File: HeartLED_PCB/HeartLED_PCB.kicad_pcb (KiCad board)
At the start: 2 copper layers, 58.8 x 52.2 mm, 35 parts, among them U1 ICM7555CBAZ, U2 CD4017BM, U3 HT7750A, U4 HX SS12F44G4

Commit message: Added LCSC and 3D models
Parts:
- C3: footprint FOOTPRINTS:TAJA476K006RNJ -> FOOTPRINTS:TAJA226M010RNJ
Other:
- board text added: "github.com/ fectec/ HeartLED"
- board text removed: "github.com/ fectec/ HeartLEDChaser"

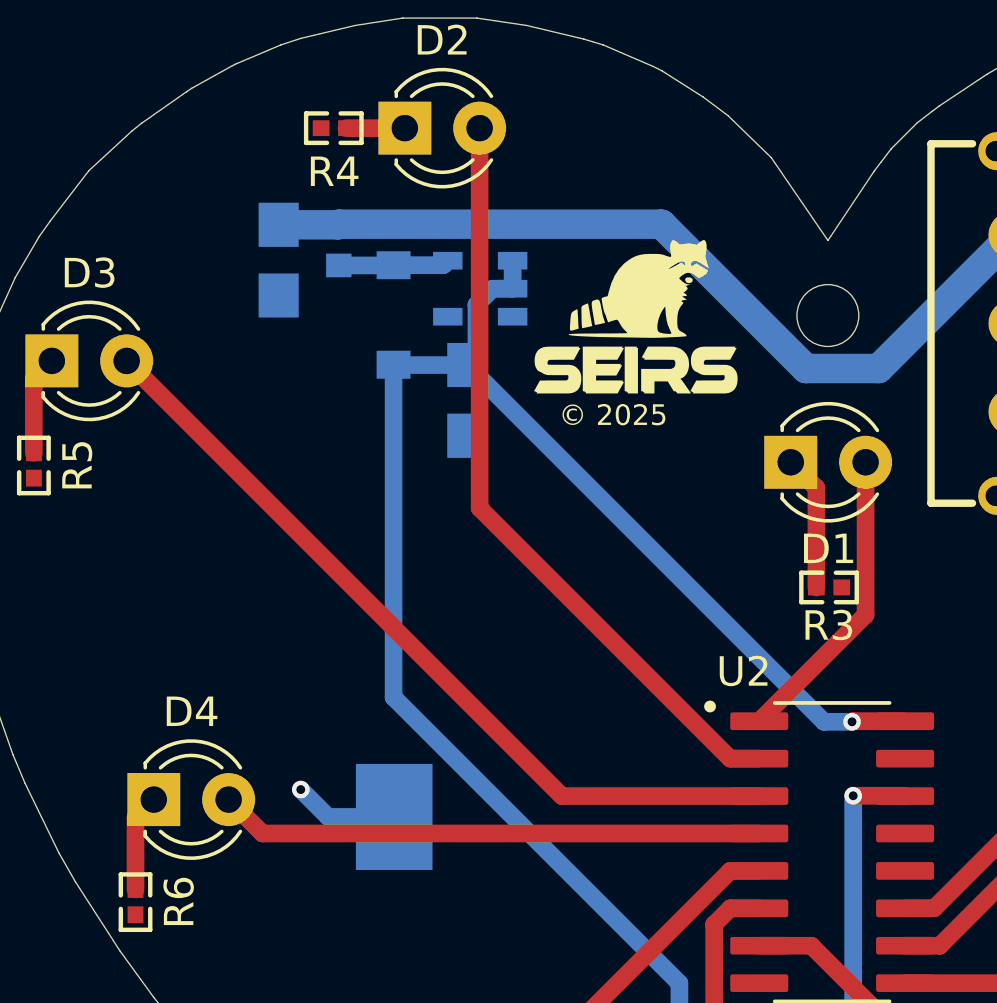
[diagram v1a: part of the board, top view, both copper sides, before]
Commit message: Changed inductor
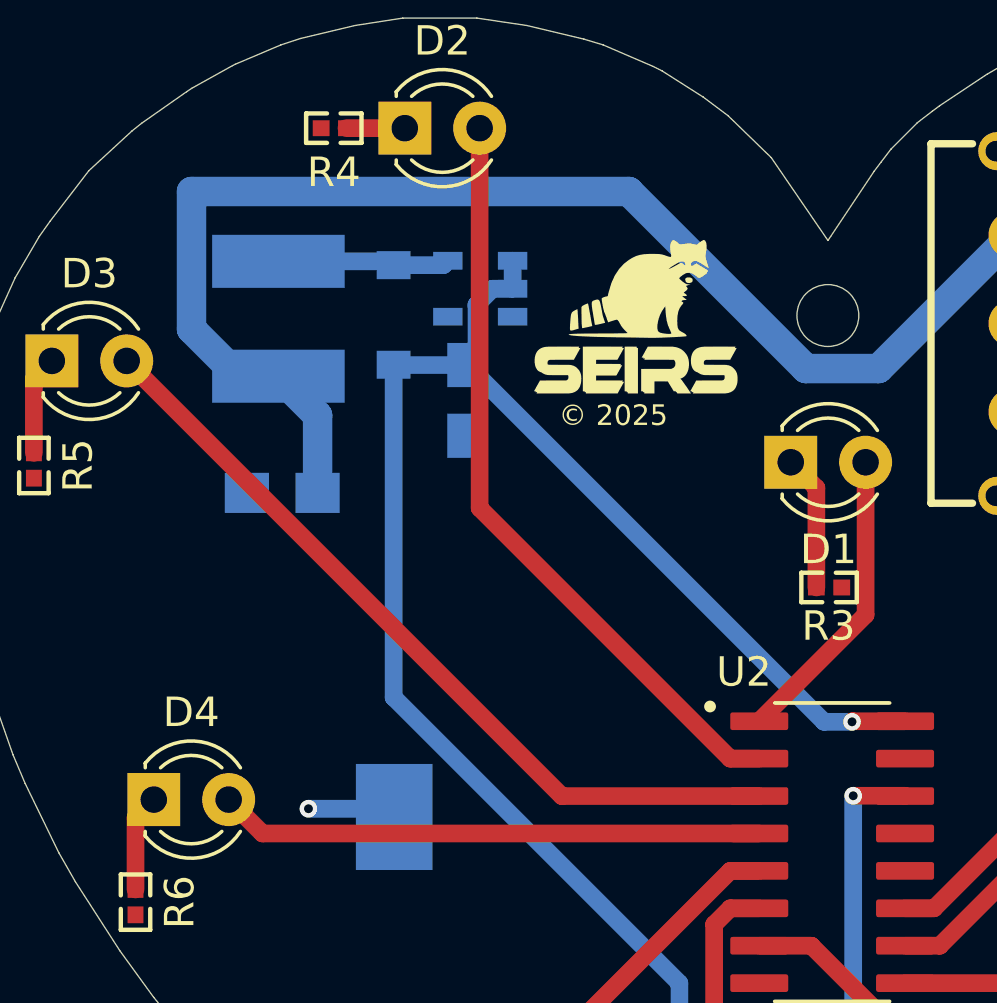
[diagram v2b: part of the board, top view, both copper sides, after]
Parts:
- L1: footprint FOOTPRINTS:SDFL1608Q4R7KTF -> FOOTPRINTS:SMNR5040-470MT
- moved C2 7.90 mm to (111.5, 88.6), turned to 180 degrees
- moved L1 3.24 mm to (111.3, 82.7), turned to 90 degrees
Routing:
- net +3V0: track 28.8 -> 43.7 mm
- net Net-(S1-A): track 3.75 -> 5.68 mm
- net GND: track 3.56 -> 3.03 mm

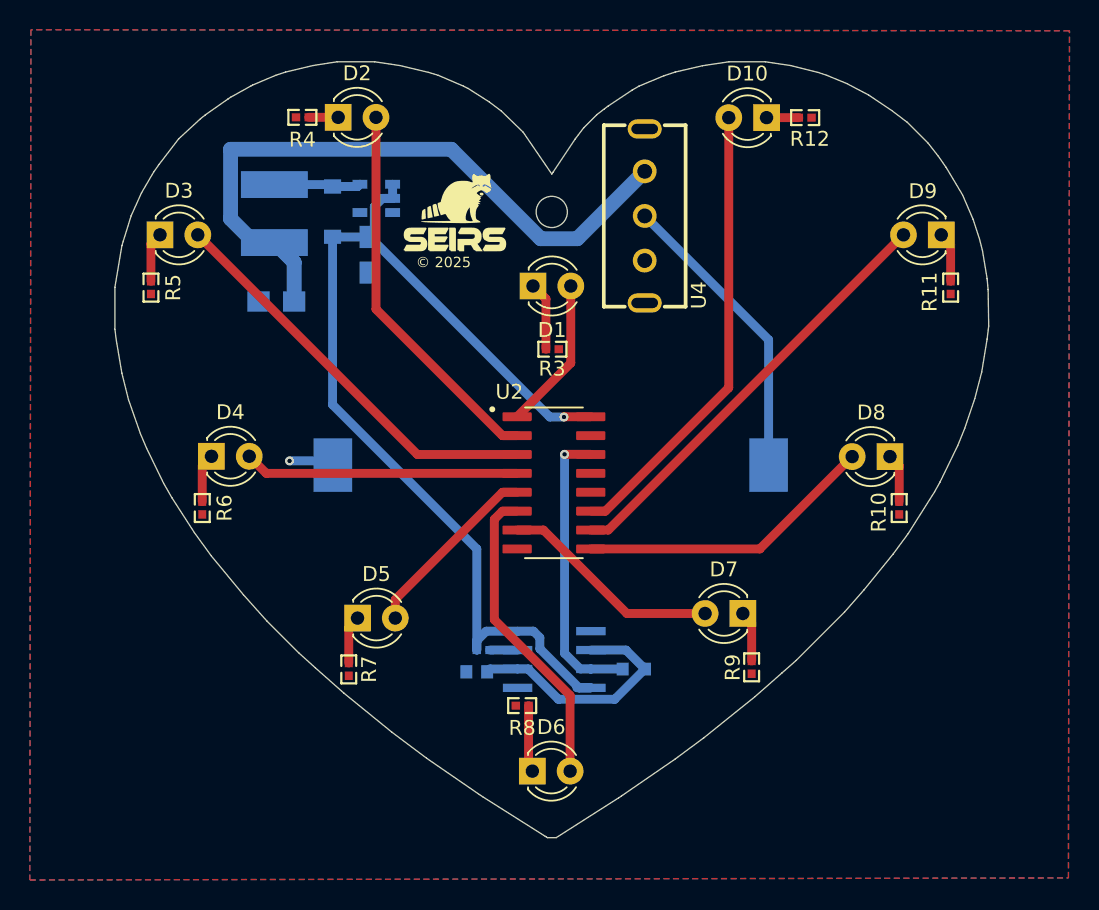
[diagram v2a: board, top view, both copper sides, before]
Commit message: Added TestPoints and corrected track width for power nets
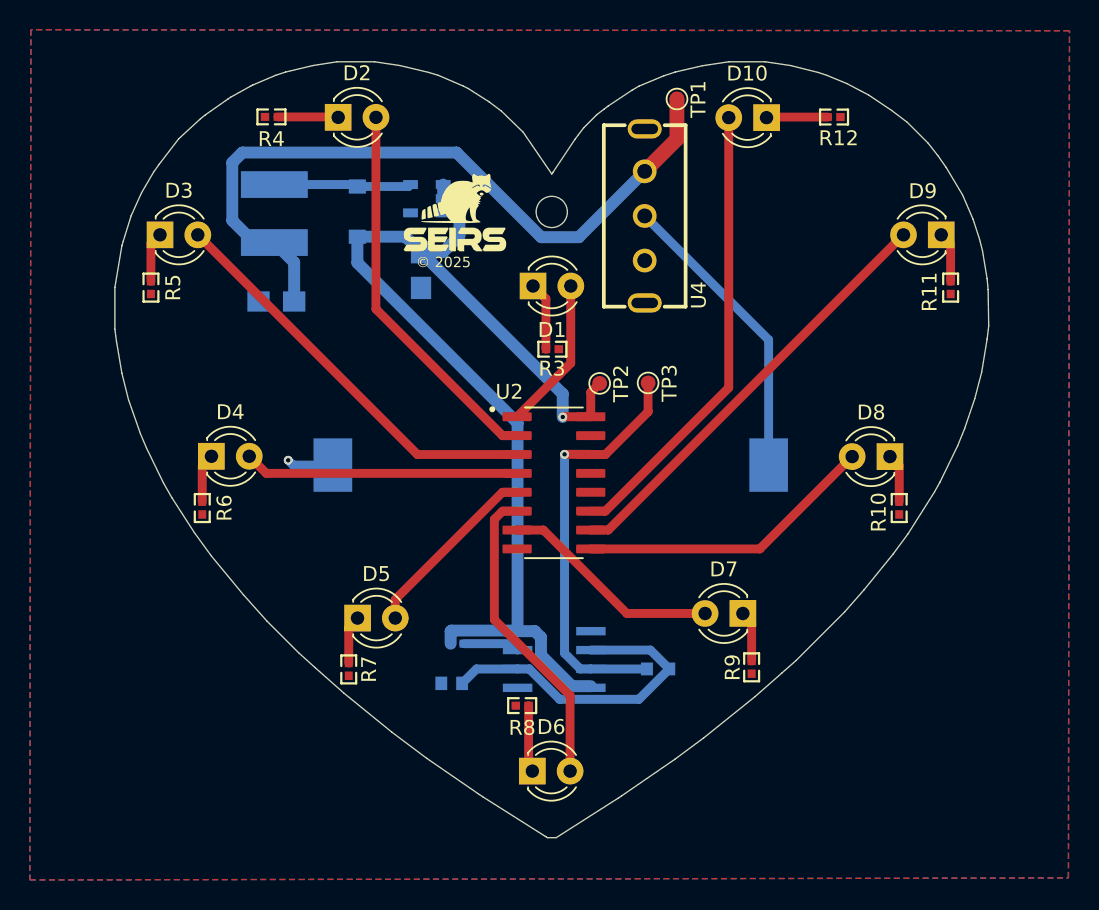
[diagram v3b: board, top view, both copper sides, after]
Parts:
- added TP1: TestPoint, TestPoint:TestPoint_Pad_D1.0mm, F.Cu at (138.4, 75.0)
- added TP2: TestPoint, TestPoint:TestPoint_Pad_D1.0mm, F.Cu at (133.2, 94.1)
- added TP3: TestPoint, TestPoint:TestPoint_Pad_D1.0mm, F.Cu at (136.5, 94.1)
- moved C3 3.60 mm to (121.2, 86.5)
- moved U3 3.40 mm to (121.6, 81.7)
- moved R4 2.08 mm to (111.2, 76.2)
- moved R12 1.94 mm to (149.0, 76.2)
- moved C1 1.86 mm to (123.3, 114.3)
- moved R2 1.79 mm to (123.7, 111.6)
- moved S1 1.67 mm to (116.9, 82.6)
- moved R1 1.63 mm to (137.2, 113.3)
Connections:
- net +3V0 renamed +3V
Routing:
- net ASTABLE_OUTPUT: track 19.5 -> 28.1 mm
- net +5V: track 69.8 -> 75.2 mm
- net Net-(U1-THRESHOLD): track 16.5 -> 21.8 mm
- net +3V: track 43.7 -> 48.5 mm
- net Net-(S1-A): track 5.68 -> 9.07 mm
- net Net-(D2-K): track 1.98 -> 4.03 mm
- net Net-(U1-DISCHARGE): track 1.88 -> 3.80 mm
- net Net-(D10-K): track 2.17 -> 4.07 mm

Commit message: Changed Timer and Counter models
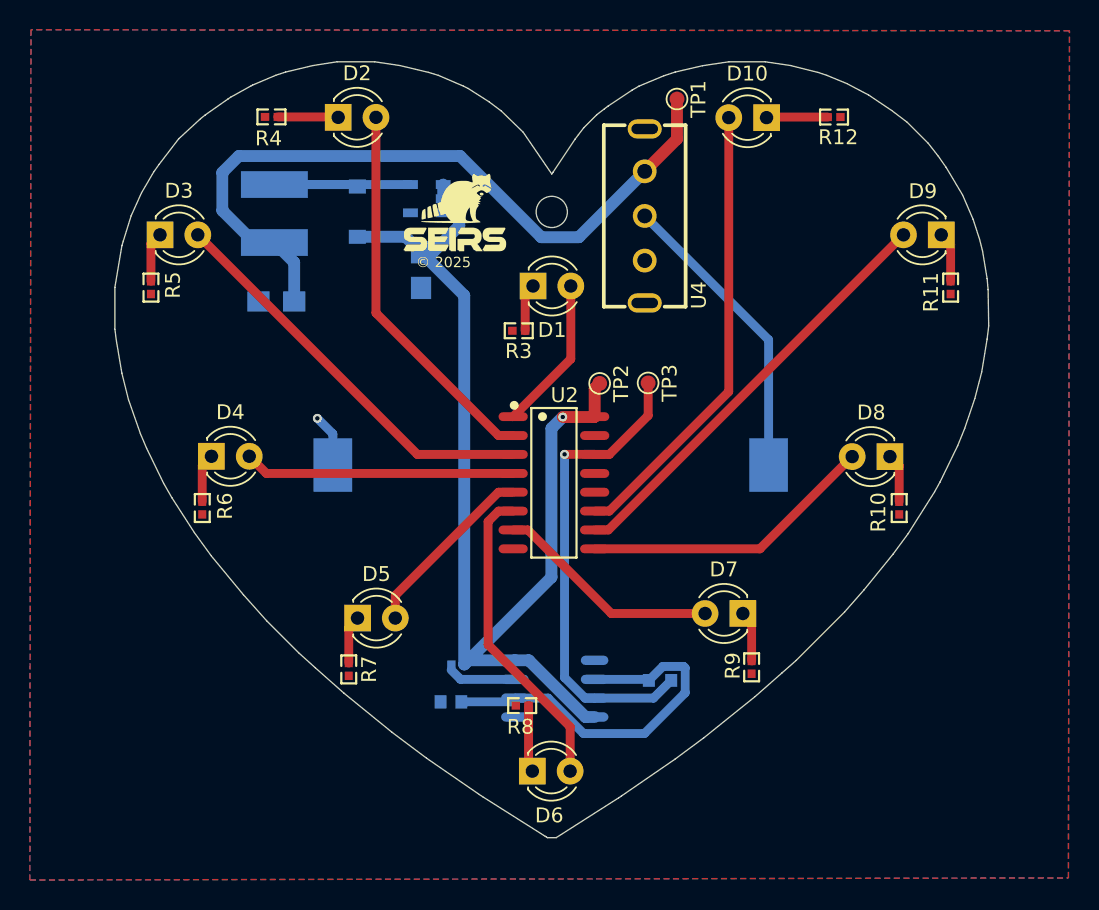
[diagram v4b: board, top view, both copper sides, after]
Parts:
- U1: value ICM7555CBAZ -> ICM7555IBAZ-T; footprint FOOTPRINTS:ICM7555CBAZ -> FOOTPRINTS:ICM7555IBAZ-T
- U2: value CD4017BM -> CD4017BM96; footprint FOOTPRINTS:CD4017BM -> FOOTPRINTS:CD4017BM96
- moved R3 2.58 mm to (127.8, 90.6), turned to 180 degrees
- moved U1 1.97 mm to (130.2, 114.7), turned to -90 degrees
- moved R2 1.40 mm to (123.7, 113.0), turned to 0 degrees
- moved C1 1.24 mm to (123.2, 115.5)
- moved R1 0.78 mm to (137.3, 114.1)
- turned R10 to 90 degrees
- turned R11 to 90 degrees
- turned R12 to 180 degrees
- turned U2 to -90 degrees
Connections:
- R1 pad 1: Net-(U1-THRESHOLD) -> ASTABLE_OUTPUT
- R1 pad 2: ASTABLE_OUTPUT -> Net-(U1-THRESHOLD)
- R10 pad 1: Net-(D8-K) -> GND
- R10 pad 2: GND -> Net-(D8-K)
- R11 pad 1: Net-(D9-K) -> GND
- R11 pad 2: GND -> Net-(D9-K)
- R12 pad 1: Net-(D10-K) -> GND
- R12 pad 2: GND -> Net-(D10-K)
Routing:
- net Net-(S1-A): track 9.07 -> 14.6 mm
- net ASTABLE_OUTPUT: track 28.1 -> 32.1 mm
- net Net-(U1-THRESHOLD): track 21.8 -> 25.4 mm
- net Net-(D1-K): track 4.61 -> 2.48 mm
- net Net-(U1-DISCHARGE): track 3.80 -> 4.55 mm
